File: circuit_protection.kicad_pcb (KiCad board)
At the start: 2 copper layers, 43 x 41 mm, 12 parts, among them J1 +VIN, J2 -VIN, J3 +VOUT, J4 -VOUT, Q1 DMP4065S, Q2 DMP4065S, Q3 PMBT2907A

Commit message: at home etch board layout
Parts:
- moved D3 13.5 mm to (180.6, 72.1), turned to 270 degrees
- moved R4 6.89 mm to (185.2, 69.8)
- moved R1 5.64 mm to (177.0, 79.9), turned to 90 degrees
- moved Q3 5.31 mm to (181.5, 68.8)
- moved D2 3.79 mm to (171.6, 78.0), turned to 90 degrees
- moved Q2 2.20 mm to (190.5, 68.8)
- moved R3 1.75 mm to (167.2, 76.1)
- moved Q1 0.21 mm to (172.5, 68.8)
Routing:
- net Net-(D2-Pad1): track 23.9 -> 38.8 mm
- net Net-(D3-Pad1): track 18.7 -> 4.80 mm
- net Net-(J1-Pad1): track 11.9 -> 0.00 mm
- net GND: track 0.00 -> 10.9 mm
- net Net-(J3-Pad1): track 9.51 -> 0.00 mm
- net Net-(D2-Pad2): track 9.07 -> 10.8 mm
- net Net-(Q2-Pad1): track 12.3 -> 10.9 mm
- added copper zone on F.Cu, net GND
- added copper zone on F.Cu, net Net-(J1-Pad1)
- added copper zone on F.Cu, net Net-(J3-Pad1)

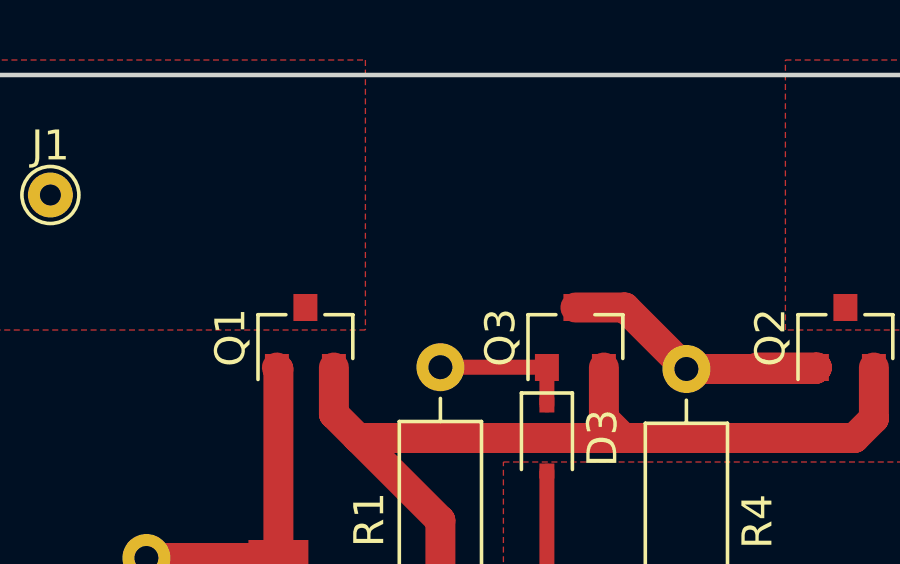
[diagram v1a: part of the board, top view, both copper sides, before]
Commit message: place new zener, not connected
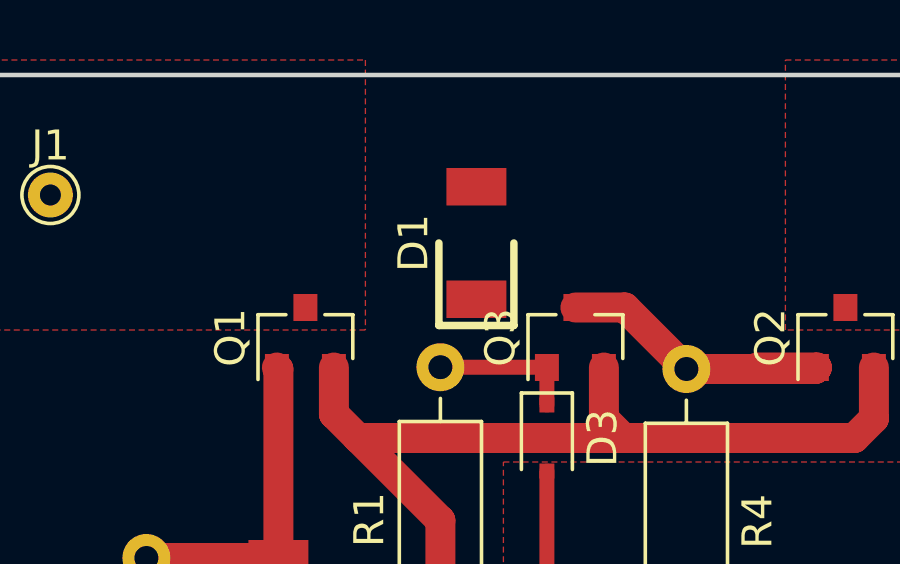
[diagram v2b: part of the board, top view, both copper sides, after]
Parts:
- added D1: 15V, Vishay:Vishay_TZM5258B_SOD80, F.Cu at (178.2, 65.6)
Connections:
- net Net-(D2-Pad1) renamed /Va
